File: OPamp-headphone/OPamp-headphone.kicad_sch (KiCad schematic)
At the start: 9 parts, among them U1 ${SIM.PARAMS}

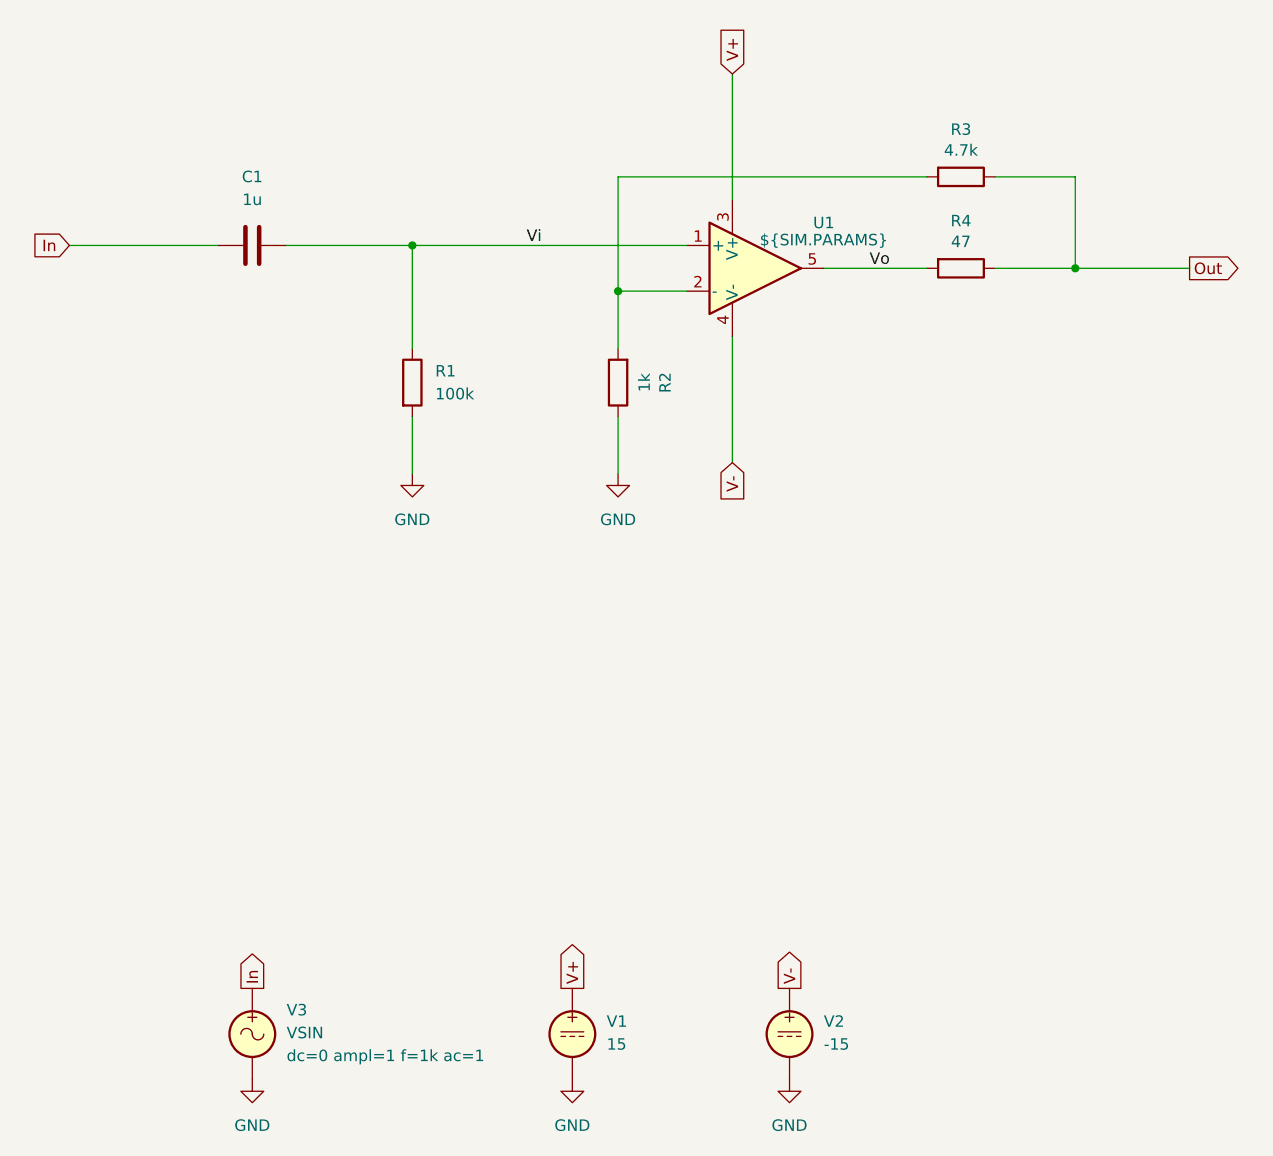
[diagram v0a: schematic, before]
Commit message: Tested/updated for KiCad 9
Schematics are tested and updated for KiCad 9, no changes in circuitry
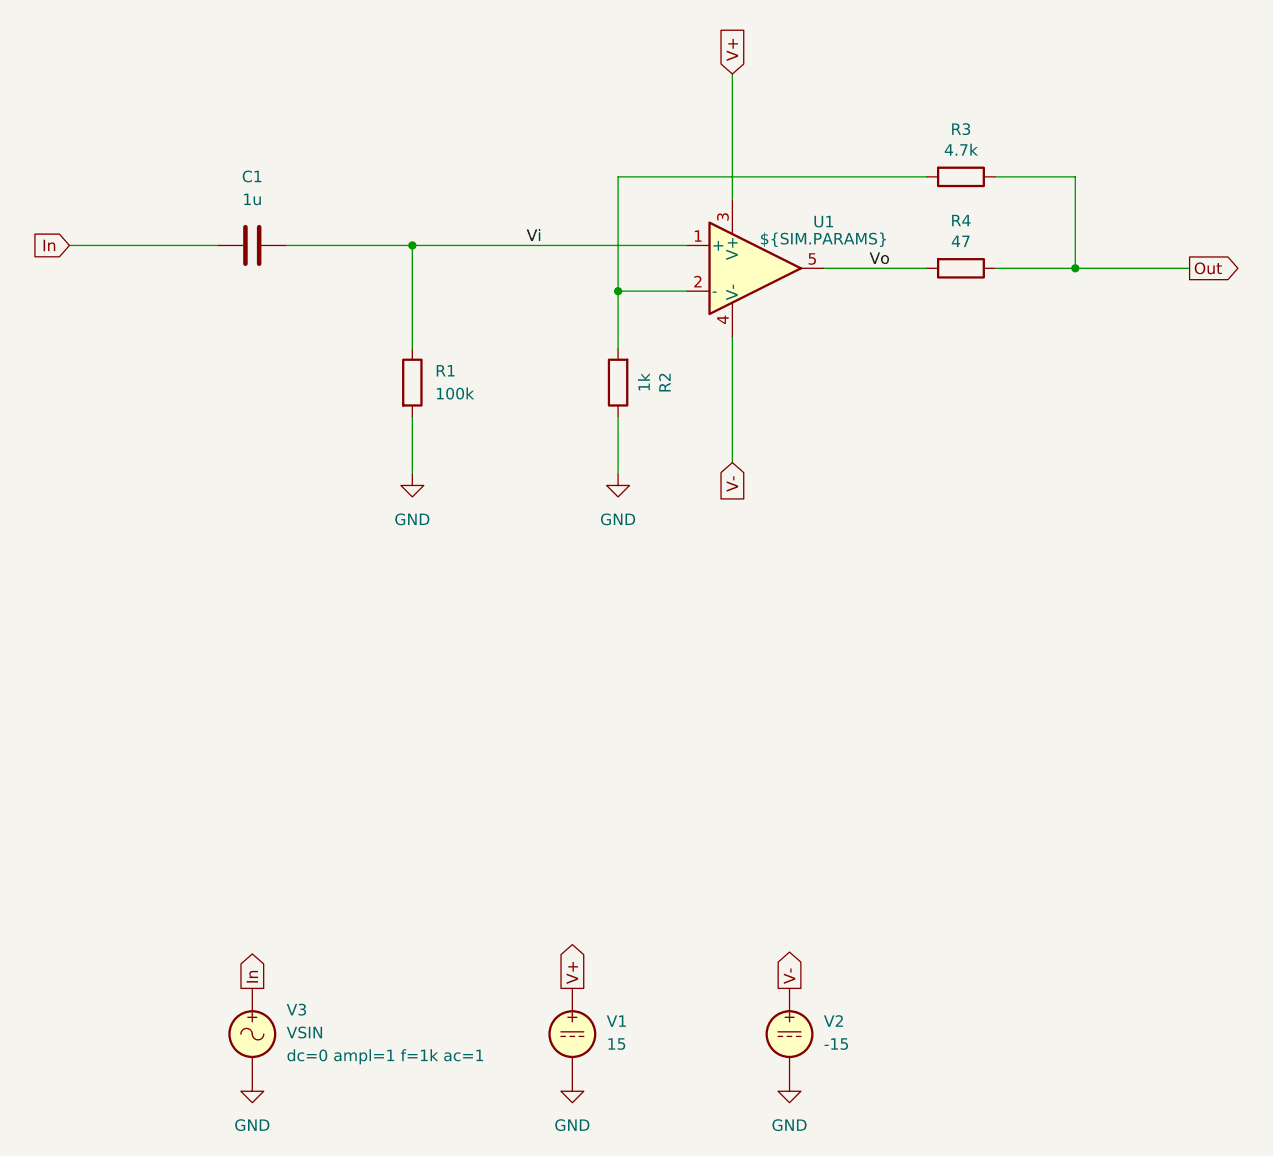
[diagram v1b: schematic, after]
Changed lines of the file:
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@@
 (kicad_sch
-	(version 20231120)
+	(version 20250114)
 	(generator "eeschema")
-	(generator_version "8.0")
+	(generator_version "9.0")
 	(paper "A4")
 	(title_block
 		(title "OPamp, headphone")
-		(date "2024-12-15")
+		(date "2025-09-13")
 		(company "GitHub/OJStuff")
 	)
@@
 	(label "Vi"
 		(at 130.81 93.98 0)
-		(fields_autoplaced yes)
 		(effects
 			(font
@@
 	(label "Vo"
 		(at 168.91 96.52 0)
-		(fields_autoplaced yes)
 		(effects
 			(font
@@
 	)
 	(symbol
+		(lib_id "Simulation_SPICE:OPAMP")
+		(at 156.21 96.52 0)
+		(unit 1)
+		(exclude_from_sim no)
+		(in_bom yes)
+		(on_board yes)
+		(dnp no)
+		(fields_autoplaced yes)
+		(property "Reference" "U1"
+			(at 163.83 91.3698 0)
+			(effects
+				(font
+					(size 1.27 1.27)
+				)
+			)
+		)
+		(property "Value" "${SIM.PARAMS}"
+			(at 163.83 93.2749 0)
+			(effects
+				(font
+					(size 1.27 1.27)
+				)
+			)
+		)
+		(property "Footprint" ""
+			(at 156.21 96.52 0)
+			(effects
+				(font
+					(size 1.27 1.27)
+				)
+				(hide yes)
+			)
+		)
+		(property "Datasheet" "https://ngspice.sourceforge.io/docs/ngspice-html-manual/manual.xhtml#sec__SUBCKT_Subcircuits"
+			(at 156.21 96.52 0)
+			(effects
+				(font
+					(size 1.27 1.27)
+				)
+				(hide yes)
+			)
+		)
+		(property "Description" "Operational amplifier, single"
+			(at 156.21 96.52 0)
+			(effects
+				(font
+					(size 1.27 1.27)
+				)
+				(hide yes)
+			)
+		)
+		(property "Sim.Pins" "1=in+ 2=in- 3=vcc 4=vee 5=out"
+			(at 156.21 96.52 0)
+			(effects
+				(font
+					(size 1.27 1.27)
+				)
+				(hide yes)
+			)
+		)
+		(property "Sim.Device" "SUBCKT"
+			(at 156.21 96.52 0)
+			(effects
+				(font
+					(size 1.27 1.27)
+				)
+				(justify left)
+				(hide yes)
+			)
+		)
+		(property "Sim.Library" "${KICAD9_SYMBOL_DIR}/Simulation_SPICE.sp"
+			(at 156.21 96.52 0)
+			(effects
+				(font
+					(size 1.27 1.27)
+				)
+				(hide yes)
+			)
+		)
+		(property "Sim.Name" "kicad_builtin_opamp"
+			(at 156.21 96.52 0)
+			(effects
+				(font
+					(size 1.27 1.27)
+				)
+				(hide yes)
+			)
+		)
+		(pin "5"
+		)
+		(pin "4"
+		)
+		(pin "3"
+		)
+		(pin "2"
+		)
+		(pin "1"
+		)
+		(instances
+			(project ""
+				(path "/a81f47c8-d758-4a1a-b078-3bf1b27e0f5d"
+					(reference "U1")
+					(unit 1)
+				)
+			)
+		)
+	)
+	(symbol
 		(lib_name "VSIN_1")
 		(lib_id "Simulation_SPICE:VSIN")
@@
 				(path "/a81f47c8-d758-4a1a-b078-3bf1b27e0f5d"
 					(reference "C1")
-					(unit 1)
-				)
-			)
-		)
-	)
-	(symbol
-		(lib_id "Simulation_SPICE:OPAMP")
-		(at 156.21 96.52 0)
-		(unit 1)
-		(exclude_from_sim no)
-		(in_bom yes)
-		(on_board yes)
-		(dnp no)
-		(fields_autoplaced yes)
-		(property "Reference" "U1"
-			(at 163.83 91.4714 0)
-			(effects
-				(font
-					(size 1.27 1.27)
-				)
-			)
-		)
-		(property "Value" "${SIM.PARAMS}"
-			(at 163.83 93.3765 0)
-			(effects
-				(font
-					(size 1.27 1.27)
-				)
-			)
-		)
-		(property "Footprint" ""
-			(at 156.21 96.52 0)
-			(effects
-				(font
-					(size 1.27 1.27)
-				)
-				(hide yes)
-			)
-		)
-		(property "Datasheet" "https://ngspice.sourceforge.io/docs/ngspice-html-manual/manual.xhtml#sec__SUBCKT_Subcircuits"
-			(at 156.21 96.52 0)
-			(effects
-				(font
-					(size 1.27 1.27)
-				)
-				(hide yes)
-			)
-		)
-		(property "Description" "Operational amplifier, single, node sequence=1:+ 2:- 3:OUT 4:V+ 5:V-"
-			(at 156.21 96.52 0)
-			(effects
-				(font
-					(size 1.27 1.27)
-				)
-				(hide yes)
-			)
-		)
-		(property "Sim.Pins" "1=in+ 2=in- 3=vcc 4=vee 5=out"
-			(at 156.21 96.52 0)
-			(effects
-				(font
-					(size 1.27 1.27)
-				)
-				(hide yes)
-			)
-		)
-		(property "Sim.Device" "SUBCKT"
-			(at 156.21 96.52 0)
-			(effects
-				(font
-					(size 1.27 1.27)
-				)
-				(justify left)
-				(hide yes)
-			)
-		)
-		(property "Sim.Library" "${KICAD7_SYMBOL_DIR}/Simulation_SPICE.sp"
-			(at 156.21 96.52 0)
-			(effects
-				(font
-					(size 1.27 1.27)
-				)
-				(hide yes)
-			)
-		)
-		(property "Sim.Name" "kicad_builtin_opamp"
-			(at 156.21 96.52 0)
-			(effects
-				(font
-					(size 1.27 1.27)
-				)
-				(hide yes)
-			)
-		)
-		(pin "2"
-		)
-		(pin "5"
-		)
-		(pin "1"
-		)
-		(pin "3"
-		)
-		(pin "4"
-		)
-		(instances
-			(project "OPamp-headphone-(.ac)"
-				(path "/a81f47c8-d758-4a1a-b078-3bf1b27e0f5d"
-					(reference "U1")
 					(unit 1)
 				)
@@
 		)
 	)
+	(embedded_fonts no)
 )
